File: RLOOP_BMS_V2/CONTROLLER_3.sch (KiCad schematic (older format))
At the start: 21 parts

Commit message: Bug Fixes
A few fixes and cleanup to make the ERC happy.
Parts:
- removed C? (x3): 100 nF / 50V/ 10% / SMD 0603, symbol C
- removed C? (x2): 100n, symbol C
- removed C?: 100n / 50V / 10% / SMD 0603, symbol C
- removed C?: 10uF / 25V / 20% / SMD 1206, symbol C
- removed R?: 121K / 0.1W / 1% / SMD 0603, symbol R
- removed R?: 10K / .1 W / 1% / SMD 0603, symbol R
- removed R?: 10, symbol R
- removed R?: 100k, symbol R
- added C30: 10uF / 25V / 20% / SMD 1206, symbol C
- added C32: 100n / 50V / 10% / SMD 0603, symbol C
- added C36, C38, C39: 100 nF / 50V/ 10% / SMD 0603, symbol C
- added C40, C41: 100n, symbol C
- added R16: 10, symbol R
- added R17: 121K / 0.1W / 1% / SMD 0603, symbol R
- added R18: 10K / .1 W / 1% / SMD 0603, symbol R
- gave numbers to parts that had none: 10
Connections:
- net labels removed: Thermal_Pad_3
- wire segments 93 -> 88
- no-connect marks 0 -> 3
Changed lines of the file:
@@
 VDDHVM
 $Comp
-L ATA6870N-PLQW-1 IC?
+L ATA6870N-PLQW-1 IC5
 U 1 1 591D6F2A
 P 5600 3400
-F 0 "IC?" H 6300 5200 60  0000 C CNN
+F 0 "IC5" H 6300 5200 60  0000 C CNN
 F 1 "ATA6870N-PLQW-1" H 6650 5100 60  0000 C CNN
 F 2 "" H 5550 3400 60  0001 C CNN
@@
 GND_3
 $Comp
-L C C?
+L C C34
 U 1 1 59101A84
 P 8350 1950
-F 0 "C?" H 8100 1950 50  0000 L CNN
+F 0 "C34" H 8100 1950 50  0000 L CNN
 F 1 "100 nF / 50V/ 10% / SMD 0603" H 8500 1950 50  0000 L CNN
 F 2 "" H 8388 1800 50  0001 C CNN
@@
 $EndComp
 $Comp
-L C C?
+L C C35
 U 1 1 59101A9B
 P 8350 2250
-F 0 "C?" H 8100 2250 50  0000 L CNN
+F 0 "C35" H 8100 2250 50  0000 L CNN
 F 1 "100 nF / 50V/ 10% / SMD 0603" H 8500 2250 50  0000 L CNN
 F 2 "" H 8388 2100 50  0001 C CNN
@@
 $EndComp
 $Comp
-L C C?
-U 1 1 59101AC2
+L C C36
+U 1 1 5917E369
 P 8350 2550
-F 0 "C?" H 8100 2550 50  0000 L CNN
+F 0 "C36" H 8100 2550 50  0000 L CNN
 F 1 "100 nF / 50V/ 10% / SMD 0603" H 8500 2550 50  0000 L CNN
 F 2 "" H 8388 2400 50  0001 C CNN
@@
 $EndComp
 $Comp
-L C C?
+L C C37
 U 1 1 59101ADD
 P 8350 2850
-F 0 "C?" H 8100 2850 50  0000 L CNN
+F 0 "C37" H 8100 2850 50  0000 L CNN
 F 1 "100 nF / 50V/ 10% / SMD 0603" H 8500 2850 50  0000 L CNN
 F 2 "" H 8388 2700 50  0001 C CNN
@@
 $EndComp
 $Comp
-L C C?
-U 1 1 59101B02
+L C C38
+U 1 1 5917E36C
 P 8350 3150
-F 0 "C?" H 8100 3150 50  0000 L CNN
+F 0 "C38" H 8100 3150 50  0000 L CNN
 F 1 "100 nF / 50V/ 10% / SMD 0603" H 8500 3150 50  0000 L CNN
 F 2 "" H 8388 3000 50  0001 C CNN
@@
 $EndComp
 $Comp
-L C C?
-U 1 1 59101B2D
+L C C39
+U 1 1 5917E36E
 P 8350 3450
-F 0 "C?" H 8100 3450 50  0000 L CNN
+F 0 "C39" H 8100 3450 50  0000 L CNN
 F 1 "100 nF / 50V/ 10% / SMD 0603" H 8500 3450 50  0000 L CNN
 F 2 "" H 8388 3300 50  0001 C CNN
@@
 $EndComp
 $Comp
-L R R?
-U 1 1 59102664
+L R R17
+U 1 1 5917E370
 P 6900 4350
-F 0 "R?" V 6980 4350 50  0000 C CNN
+F 0 "R17" V 6980 4350 50  0000 C CNN
 F 1 "121K / 0.1W / 1% / SMD 0603" V 7050 4850 50  0000 C CNN
 F 2 "" V 6830 4350 50  0001 C CNN
@@
 GND_3
 $Comp
-L R R?
+L R R19
 U 1 1 591040ED
 P 9950 4050
-F 0 "R?" V 10030 4050 50  0000 C CNN
+F 0 "R19" V 10030 4050 50  0000 C CNN
 F 1 "10K / .1 W / 1% / SMD 0603" H 9300 4050 50  0000 C CNN
 F 2 "" V 9880 4050 50  0001 C CNN
@@
 $EndComp
 $Comp
-L Thermistor_NTC TH?
+L Thermistor_NTC TH6
 U 1 1 59104176
 P 9950 4550
-F 0 "TH?" V 9775 4550 50  0000 C CNN
+F 0 "TH6" V 9775 4550 50  0000 C CNN
 F 1 "NTCS0603E3103JLT" H 10450 4550 50  0000 C CNN
 F 2 "" H 9950 4600 50  0001 C CNN
@@
 $EndComp
 $Comp
-L Thermistor_NTC TH?
+L Thermistor_NTC TH5
 U 1 1 5910419D
 P 9000 4550
-F 0 "TH?" V 8825 4550 50  0000 C CNN
+F 0 "TH5" V 8825 4550 50  0000 C CNN
 F 1 "NTCS0603E3103JLT" H 9000 4350 50  0000 C CNN
 F 2 "" H 9000 4600 50  0001 C CNN
@@
 $EndComp
 $Comp
-L R R?
-U 1 1 591041CA
+L R R18
+U 1 1 5917E379
 P 9000 4050
-F 0 "R?" V 9080 4050 50  0000 C CNN
+F 0 "R18" V 9080 4050 50  0000 C CNN
 F 1 "10K / .1 W / 1% / SMD 0603" H 9200 4200 50  0000 C CNN
 F 2 "" V 8930 4050 50  0001 C CNN
@@
 GND_3
 $Comp
-L C C?
-U 1 1 59105042
+L C C41
+U 1 1 5917E37A
 P 9550 4550
-F 0 "C?" H 9575 4650 50  0000 L CNN
+F 0 "C41" H 9575 4650 50  0000 L CNN
 F 1 "100n" H 9250 4550 50  0000 L CNN
 F 2 "" H 9588 4400 50  0001 C CNN
@@
 $EndComp
 $Comp
-L C C?
-U 1 1 591051E7
+L C C40
+U 1 1 5917E37C
 P 8450 4550
-F 0 "C?" H 8475 4650 50  0000 L CNN
+F 0 "C40" H 8475 4650 50  0000 L CNN
 F 1 "100n" H 8200 4450 50  0000 L CNN
 F 2 "" H 8488 4400 50  0001 C CNN
@@
 $EndComp
 $Comp
-L R R?
-U 1 1 5910D275
+L R R16
+U 1 1 5917E380
 P 2650 6900
-F 0 "R?" V 2730 6900 50  0000 C CNN
+F 0 "R16" V 2730 6900 50  0000 C CNN
 F 1 "10" V 2650 6900 50  0000 C CNN
 F 2 "" V 2580 6900 50  0001 C CNN
@@
 $EndComp
 $Comp
-L C C?
+L C C33
 U 1 1 5910D5BF
 P 6750 2000
-F 0 "C?" H 6775 2100 50  0000 L CNN
+F 0 "C33" H 6775 2100 50  0000 L CNN
 F 1 "100nF / 50V / 10% / SMD 0603" H 5400 2150 50  0000 L CNN
 F 2 "" H 6788 1850 50  0001 C CNN
@@
 $EndComp
 $Comp
-L C C?
-U 1 1 5910D5FC
+L C C30
+U 1 1 5917E384
 P 3200 7150
-F 0 "C?" H 3225 7250 50  0000 L CNN
+F 0 "C30" H 3225 7250 50  0000 L CNN
 F 1 "10uF / 25V / 20% / SMD 1206" H 1750 7150 50  0000 L CNN
 F 2 "" H 3238 7000 50  0001 C CNN
@@
 Text GLabel 4100 3050 0    60   Input ~ 0
 VDDHV_3
-Text GLabel 3400 4550 0    60   Input ~ 0
-GND_3
-$Comp
-L R R?
-U 1 1 591108C7
-P 4200 4850
-F 0 "R?" V 4100 4850 50  0000 C CNN
-F 1 "100k" V 4200 4850 50  0000 C CNN
-F 2 "" V 4130 4850 50  0001 C CNN
-F 3 "" H 4200 4850 50  0001 C CNN
-	1    4200 4850
-	0    1    1    0
-$EndComp
-$Comp
-L C C?
-U 1 1 5910B934
+$Comp
+L C C32
+U 1 1 5917E37F
 P 5450 1700
-F 0 "C?" H 5475 1800 50  0000 L CNN
+F 0 "C32" H 5475 1800 50  0000 L CNN
 F 1 "100n / 50V / 10% / SMD 0603" H 5250 1900 50  0000 L CNN
 F 2 "" H 5488 1550 50  0001 C CNN
@@
 Text GLabel 4100 2550 0    60   Input ~ 0
 VDDHV_3
-Text Label 5200 6000 1    60   ~ 0
-Thermal_Pad_3
 Text GLabel 6750 1750 1    60   Input ~ 0
 GND_3
 $Comp
-L C C?
+L C C31
 U 1 1 59119745
 P 3250 2800
-F 0 "C?" H 3275 2900 50  0000 L CNN
+F 0 "C31" H 3275 2900 50  0000 L CNN
 F 1 "100nF / 50V / 10% / SMD 0603" H 3275 2700 50  0000 L CNN
 F 2 "" H 3288 2650 50  0001 C CNN
@@
 	4450 3550 4300 3550
 Connection ~ 4300 3550
-Wire Wire Line
-	3400 4550 4450 4550
 Connection ~ 5850 5450
-Wire Wire Line
-	4450 4750 4350 4750
-Wire Wire Line
-	4350 4750 4350 4550
-Connection ~ 4350 4550
-Wire Wire Line
-	4450 4850 4350 4850
-Wire Wire Line
-	4050 4850 4000 4850
-Wire Wire Line
-	4000 4850 4000 4550
-Connection ~ 4000 4550
-Wire Wire Line
-	4450 4950 3850 4950
-Wire Wire Line
-	3850 4950 3850 4550
-Connection ~ 3850 4550
 Wire Wire Line
 	4300 1850 5650 1850
@@
 	4100 2550 4450 2550
 Wire Wire Line
-	5250 5300 5250 6000
-Wire Wire Line
 	6650 3800 9950 3800
 Wire Wire Line
@@
 Connection ~ 9000 5100
 Wire Wire Line
-	5250 6000 5200 6000
-Wire Wire Line
 	6750 2150 6750 2200
 Connection ~ 6750 2200
@@
 Connection ~ 3250 2650
 $Comp
-L C C?
+L C C29
 U 1 1 5911BED4
 P 2700 2800
-F 0 "C?" H 2725 2900 50  0000 L CNN
+F 0 "C29" H 2725 2900 50  0000 L CNN
 F 1 "10uF / 25V / 20% / SMD 1206" H 1300 2800 50  0000 L CNN
 F 2 "" H 2738 2650 50  0001 C CNN
@@
 	2400 2950 3250 2950
 Connection ~ 2700 2950
+Wire Wire Line
+	4100 4550 4450 4550
+Text GLabel 4100 4550 0    60   Input ~ 0
+GND_3
+NoConn ~ 4450 4750
+NoConn ~ 4450 4850
+NoConn ~ 4450 4950
+Text GLabel 12350 3700 0    60   Input ~ 0
+GND_3
+Text GLabel 12350 4050 0    60   Input ~ 0
+VDDHV_3
+$Comp
+L PWR_FLAG #FLG05
+U 1 1 59192918
+P 12650 3400
+F 0 "#FLG05" H 12650 3475 50  0001 C CNN
+F 1 "PWR_FLAG" H 12650 3550 50  0000 C CNN
+F 2 "" H 12650 3400 50  0001 C CNN
+F 3 "" H 12650 3400 50  0001 C CNN
+	1    12650 3400
+	1    0    0    -1
+$EndComp
+$Comp
+L PWR_FLAG #FLG06
+U 1 1 59192954
+P 13250 3400
+F 0 "#FLG06" H 13250 3475 50  0001 C CNN
+F 1 "PWR_FLAG" H 13250 3550 50  0000 C CNN
+F 2 "" H 13250 3400 50  0001 C CNN
+F 3 "" H 13250 3400 50  0001 C CNN
+	1    13250 3400
+	1    0    0    -1
+$EndComp
+Wire Wire Line
+	13250 3400 13250 4050
+Wire Wire Line
+	13250 4050 12350 4050
+Wire Wire Line
+	12650 3400 12650 3700
+Wire Wire Line
+	12650 3700 12350 3700
 $EndSCHEMATC

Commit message: Footprint work
starting to assign footprints to parts
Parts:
- C29, C30: footprint (none) -> Capacitors_SMD:C_1206
- C31, C32, C33, C34, C35, C36, C37, C38, C39, C40, C41: footprint (none) -> Capacitors_SMD:C_0603
- R16, R17, R18, R19: footprint (none) -> Resistors_SMD:R_0603
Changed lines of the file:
@@
 F 0 "C34" H 8100 1950 50  0000 L CNN
 F 1 "100 nF / 50V/ 10% / SMD 0603" H 8500 1950 50  0000 L CNN
-F 2 "" H 8388 1800 50  0001 C CNN
+F 2 "Capacitors_SMD:C_0603" H 8388 1800 50  0001 C CNN
 F 3 "" H 8350 1950 50  0001 C CNN
 	1    8350 1950
@@
 F 0 "C35" H 8100 2250 50  0000 L CNN
 F 1 "100 nF / 50V/ 10% / SMD 0603" H 8500 2250 50  0000 L CNN
-F 2 "" H 8388 2100 50  0001 C CNN
+F 2 "Capacitors_SMD:C_0603" H 8388 2100 50  0001 C CNN
 F 3 "" H 8350 2250 50  0001 C CNN
 	1    8350 2250
@@
 F 0 "C36" H 8100 2550 50  0000 L CNN
 F 1 "100 nF / 50V/ 10% / SMD 0603" H 8500 2550 50  0000 L CNN
-F 2 "" H 8388 2400 50  0001 C CNN
+F 2 "Capacitors_SMD:C_0603" H 8388 2400 50  0001 C CNN
 F 3 "" H 8350 2550 50  0001 C CNN
 	1    8350 2550
@@
 F 0 "C37" H 8100 2850 50  0000 L CNN
 F 1 "100 nF / 50V/ 10% / SMD 0603" H 8500 2850 50  0000 L CNN
-F 2 "" H 8388 2700 50  0001 C CNN
+F 2 "Capacitors_SMD:C_0603" H 8388 2700 50  0001 C CNN
 F 3 "" H 8350 2850 50  0001 C CNN
 	1    8350 2850
@@
 F 0 "C38" H 8100 3150 50  0000 L CNN
 F 1 "100 nF / 50V/ 10% / SMD 0603" H 8500 3150 50  0000 L CNN
-F 2 "" H 8388 3000 50  0001 C CNN
+F 2 "Capacitors_SMD:C_0603" H 8388 3000 50  0001 C CNN
 F 3 "" H 8350 3150 50  0001 C CNN
 	1    8350 3150
@@
 F 0 "C39" H 8100 3450 50  0000 L CNN
 F 1 "100 nF / 50V/ 10% / SMD 0603" H 8500 3450 50  0000 L CNN
-F 2 "" H 8388 3300 50  0001 C CNN
+F 2 "Capacitors_SMD:C_0603" H 8388 3300 50  0001 C CNN
 F 3 "" H 8350 3450 50  0001 C CNN
 	1    8350 3450
@@
 F 0 "R17" V 6980 4350 50  0000 C CNN
 F 1 "121K / 0.1W / 1% / SMD 0603" V 7050 4850 50  0000 C CNN
-F 2 "" V 6830 4350 50  0001 C CNN
+F 2 "Resistors_SMD:R_0603" V 6830 4350 50  0001 C CNN
 F 3 "" H 6900 4350 50  0001 C CNN
 	1    6900 4350
@@
 F 0 "R19" V 10030 4050 50  0000 C CNN
 F 1 "10K / .1 W / 1% / SMD 0603" H 9300 4050 50  0000 C CNN
-F 2 "" V 9880 4050 50  0001 C CNN
+F 2 "Resistors_SMD:R_0603" V 9880 4050 50  0001 C CNN
 F 3 "" H 9950 4050 50  0001 C CNN
 	1    9950 4050
@@
 F 0 "R18" V 9080 4050 50  0000 C CNN
 F 1 "10K / .1 W / 1% / SMD 0603" H 9200 4200 50  0000 C CNN
-F 2 "" V 8930 4050 50  0001 C CNN
+F 2 "Resistors_SMD:R_0603" V 8930 4050 50  0001 C CNN
 F 3 "" H 9000 4050 50  0001 C CNN
 	1    9000 4050
@@
 F 0 "C41" H 9575 4650 50  0000 L CNN
 F 1 "100n" H 9250 4550 50  0000 L CNN
-F 2 "" H 9588 4400 50  0001 C CNN
+F 2 "Capacitors_SMD:C_0603" H 9588 4400 50  0001 C CNN
 F 3 "" H 9550 4550 50  0001 C CNN
 	1    9550 4550
@@
 F 0 "C40" H 8475 4650 50  0000 L CNN
 F 1 "100n" H 8200 4450 50  0000 L CNN
-F 2 "" H 8488 4400 50  0001 C CNN
+F 2 "Capacitors_SMD:C_0603" H 8488 4400 50  0001 C CNN
 F 3 "" H 8450 4550 50  0001 C CNN
 	1    8450 4550
@@
 F 0 "R16" V 2730 6900 50  0000 C CNN
 F 1 "10" V 2650 6900 50  0000 C CNN
-F 2 "" V 2580 6900 50  0001 C CNN
+F 2 "Resistors_SMD:R_0603" V 2580 6900 50  0001 C CNN
 F 3 "" H 2650 6900 50  0001 C CNN
 	1    2650 6900
@@
 F 0 "C33" H 6775 2100 50  0000 L CNN
 F 1 "100nF / 50V / 10% / SMD 0603" H 5400 2150 50  0000 L CNN
-F 2 "" H 6788 1850 50  0001 C CNN
+F 2 "Capacitors_SMD:C_0603" H 6788 1850 50  0001 C CNN
 F 3 "" H 6750 2000 50  0001 C CNN
 	1    6750 2000
@@
 F 0 "C30" H 3225 7250 50  0000 L CNN
 F 1 "10uF / 25V / 20% / SMD 1206" H 1750 7150 50  0000 L CNN
-F 2 "" H 3238 7000 50  0001 C CNN
+F 2 "Capacitors_SMD:C_1206" H 3238 7000 50  0001 C CNN
 F 3 "" H 3200 7150 50  0001 C CNN
 	1    3200 7150
@@
 F 0 "C32" H 5475 1800 50  0000 L CNN
 F 1 "100n / 50V / 10% / SMD 0603" H 5250 1900 50  0000 L CNN
-F 2 "" H 5488 1550 50  0001 C CNN
+F 2 "Capacitors_SMD:C_0603" H 5488 1550 50  0001 C CNN
 F 3 "" H 5450 1700 50  0001 C CNN
 	1    5450 1700
@@
 F 0 "C31" H 3275 2900 50  0000 L CNN
 F 1 "100nF / 50V / 10% / SMD 0603" H 3275 2700 50  0000 L CNN
-F 2 "" H 3288 2650 50  0001 C CNN
+F 2 "Capacitors_SMD:C_0603" H 3288 2650 50  0001 C CNN
 F 3 "" H 3250 2800 50  0001 C CNN
 	1    3250 2800
@@
 F 0 "C29" H 2725 2900 50  0000 L CNN
 F 1 "10uF / 25V / 20% / SMD 1206" H 1300 2800 50  0000 L CNN
-F 2 "" H 2738 2650 50  0001 C CNN
+F 2 "Capacitors_SMD:C_1206" H 2738 2650 50  0001 C CNN
 F 3 "" H 2700 2800 50  0001 C CNN
 	1    2700 2800

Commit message: footprint and layout work WIP
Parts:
- IC5: footprint (none) -> rLoop_Footprints:ATA6870-QFN48
- TH5, TH6: footprint (none) -> Resistors_SMD:R_0603
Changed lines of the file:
@@
 F 0 "IC5" H 6300 5200 60  0000 C CNN
 F 1 "ATA6870N-PLQW-1" H 6650 5100 60  0000 C CNN
-F 2 "" H 5550 3400 60  0001 C CNN
+F 2 "rLoop_Footprints:ATA6870-QFN48" H 5550 3400 60  0001 C CNN
 F 3 "" H 5550 3400 60  0001 C CNN
 	1    5600 3400
@@
 F 0 "TH6" V 9775 4550 50  0000 C CNN
 F 1 "NTCS0603E3103JLT" H 10450 4550 50  0000 C CNN
-F 2 "" H 9950 4600 50  0001 C CNN
+F 2 "Resistors_SMD:R_0603" H 9950 4600 50  0001 C CNN
 F 3 "" H 9950 4600 50  0001 C CNN
 	1    9950 4550
@@
 F 0 "TH5" V 8825 4550 50  0000 C CNN
 F 1 "NTCS0603E3103JLT" H 9000 4350 50  0000 C CNN
-F 2 "" H 9000 4600 50  0001 C CNN
+F 2 "Resistors_SMD:R_0603" H 9000 4600 50  0001 C CNN
 F 3 "" H 9000 4600 50  0001 C CNN
 	1    9000 4550

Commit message: WIP
See if it's even possible
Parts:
- removed C29, C30: 10uF / 25V / 20% / SMD 1206, Capacitors_SMD:C_1206, symbol C
- removed C31, C33: 100nF / 50V / 10% / SMD 0603, Capacitors_SMD:C_0603, symbol C
- removed C40, C41: 100n, Capacitors_SMD:C_0603, symbol C
- removed IC5: ATA6870N-PLQW-1, rLoop_Footprints:ATA6870-QFN48, symbol ATA6870N-PLQW-1
- removed R16: 10, Resistors_SMD:R_0603, symbol R
- removed R17: 121K / 0.1W / 1% / SMD 0603, Resistors_SMD:R_0603, symbol R
- removed R18, R19: 10K / .1 W / 1% / SMD 0603, Resistors_SMD:R_0603, symbol R
- removed TH5, TH6: NTCS0603E3103JLT, Resistors_SMD:R_0603, symbol Thermistor_NTC
- added C1, C2: 2.2 uF / 50V/ 10% / SMD 0603, symbol C
- added R1: 1K0 / 0.063W / 1% / SMD 0603, symbol R
- added U1: bq76PL536A_HTQFP, symbol bq76PL536A_HTQFP
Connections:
- net labels added: 5V_3, SCLK_S, SDI_S, SDO_S
- net labels removed: CLK_IN, IRQ_OUT, SPI_MISO_LWR, SPI_MOSI_LWR, SPI_NCS_LWR, SPI_SCK_LWR, VDDHVM, ~PD_IN, ~PD_OUT
- wire segments 88 -> 74
- no-connect marks 3 -> 10
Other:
- moved on the sheet: C32, C34, C35, C36, C37, C38, C39

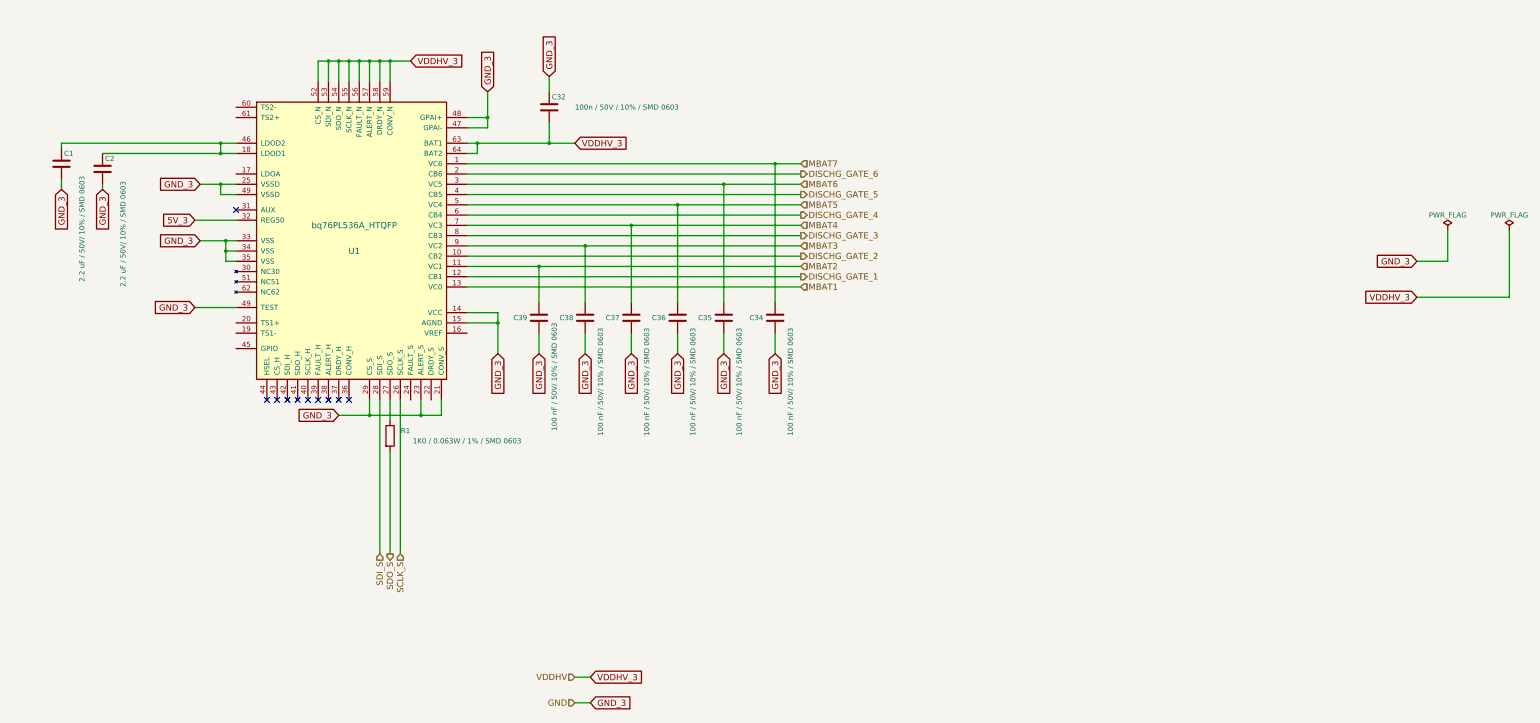
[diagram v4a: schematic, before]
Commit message: Ti BMS WIP
Getting there. Need to add temp sensors, fan control, and an LDO for the
SPI ISO supply.
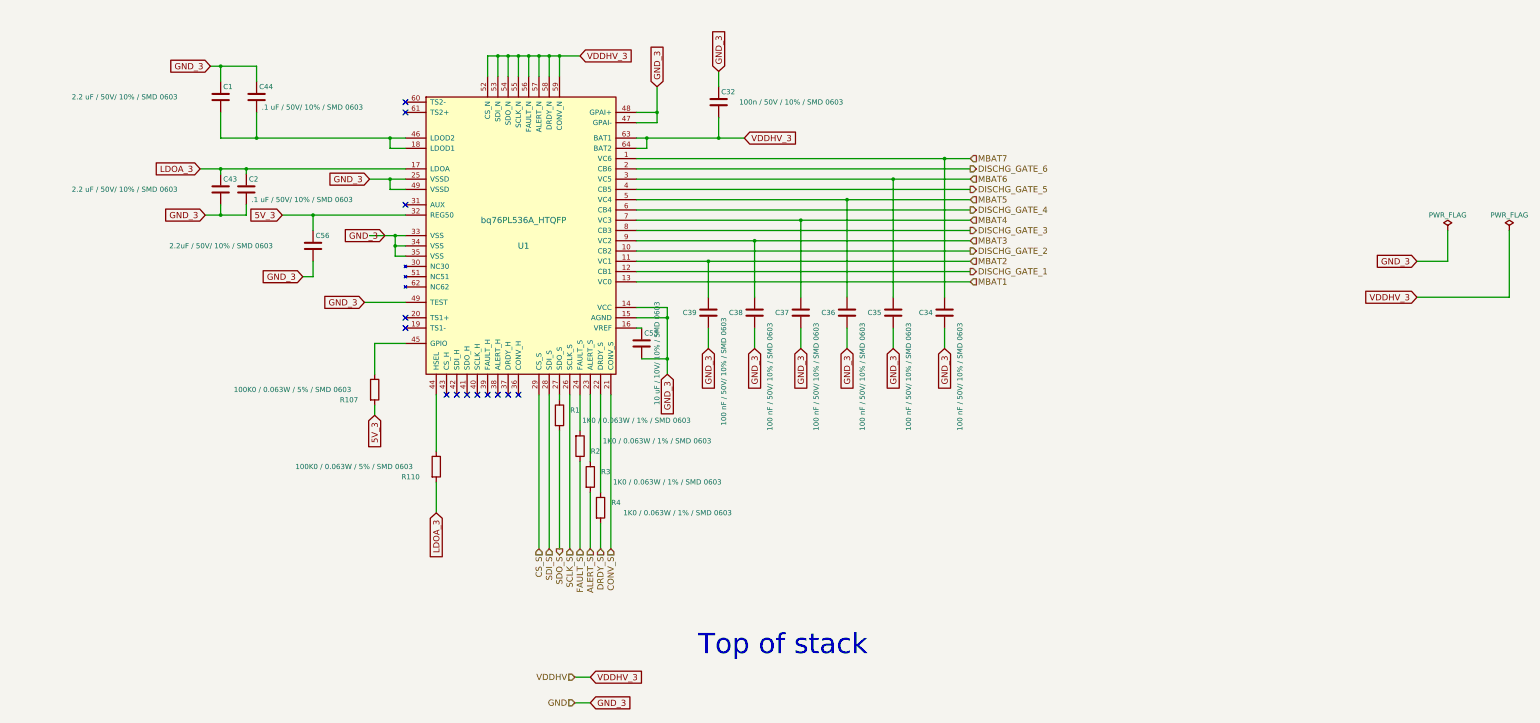
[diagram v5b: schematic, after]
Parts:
- added C43: 2.2 uF / 50V/ 10% / SMD 0603, Capacitors_SMD:C_0603, symbol C
- added C44: .1 uF / 50V/ 10% / SMD 0603, Capacitors_SMD:C_0603, symbol C
- added C53: 10 uF / 10V/ 10% / SMD 0603, Capacitors_SMD:C_0603, symbol C
- added C56: 2.2uF / 50V/ 10% / SMD 0603, Capacitors_SMD:C_0603, symbol C
- added R107, R110: 100K0 / 0.063W / 5% / SMD 0603, Resistors_SMD:R_0603, symbol R
- added R2, R3, R4: 1K0 / 0.063W / 1% / SMD 0603, Resistors_SMD:R_0603, symbol R
- C1: footprint (none) -> Capacitors_SMD:C_0603
- C2: value 2.2 uF / 50V/ 10% / SMD 0603 -> .1 uF / 50V/ 10% / SMD 0603; footprint (none) -> Capacitors_SMD:C_0603
- R1: footprint (none) -> Resistors_SMD:R_0603
- U1: footprint (none) -> rLoop_Footprints:bq76pl536a
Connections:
- net 5V_3: now also C56.1, R107.2
- net GND_3: now also C1.1, C43.2, C44.1, C53.2, C56.2; no longer C1.2, U1.21 (CONV_S), U1.23 (ALERT_S), U1.29 (CS_S)
- net at U1.16 (VREF): now also C53.1
- net LDOA_3: now reaches U1.17 (LDOA)
- net LDOA_3: now also C2.1, C43.1, R110.2
- net at U1.18 (LDOD1), U1.46 (LDOD2): now also C1.2, C44.2; no longer C1.1, C2.1
- net at U1.22 (DRDY_S): now also R4.1
- net at U1.24 (FAULT_S): now also R2.2
- net at U1.44 (HSEL): now also R110.1
- net at U1.45 (GPIO): now also R107.1
- new net: R3.1, U1.23 (ALERT_S)
- new net ALERT_S: R3.2
- new net CONV_S: U1.21 (CONV_S)
- new net CS_S: U1.29 (CS_S)
- new net DRDY_S: R4.2
- new net FAULT_S: R2.1
- no-connect marks 10 -> 13
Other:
- note added: "Top of stack"
- moved on the sheet: C1, C2, C32, C34, C35, C36, C37, C38, C39, R1, U1

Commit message: More WIP on BMS v2.5
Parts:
- added C? (x2): .047 uF / 50V/ 10% / SMD 0603, Capacitors_SMD:C_0603, symbol C
- added R? (x2): 1.82k / 0.063W / 1% / SMD 0603, symbol R
- added R? (x2): 1.47k / 0.063W / 1% / SMD 0603, symbol R
- added TH? (x2): 10k / 1% / 3454K / SMD0603, symbol Thermistor_NTC
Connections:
- net 5V_3: now also C?.1, C?.2, TH?.1, TH?.2
- net at U1.19 (TS1-): now also R?.1
- net at U1.20 (TS1+): now also C?.1, R?.1, R?.2
- net at U1.60 (TS2-): now also R?.1
- net at U1.61 (TS2+): now also C?.2, R?.1, R?.2
- new net: R?.2, TH?.2
- new net: R?.2, TH?.1
- no-connect marks 13 -> 9
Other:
- moved on the sheet: C1, C44, R107
